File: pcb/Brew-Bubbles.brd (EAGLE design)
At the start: 25.6 x 34.2 mm, 7 parts, among them U1 GP1A57HR

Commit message: JsonConfig working (mostly)
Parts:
- renumbered AMBIENT to ROOM
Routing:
- net 3V3: track 86.2 -> 90.4 mm
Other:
- board size 25.6 x 34.2 mm -> 25.5 x 28.7 mm
- board text added: "Brew Bubbles by @LBussy www.brewbubbles.com"

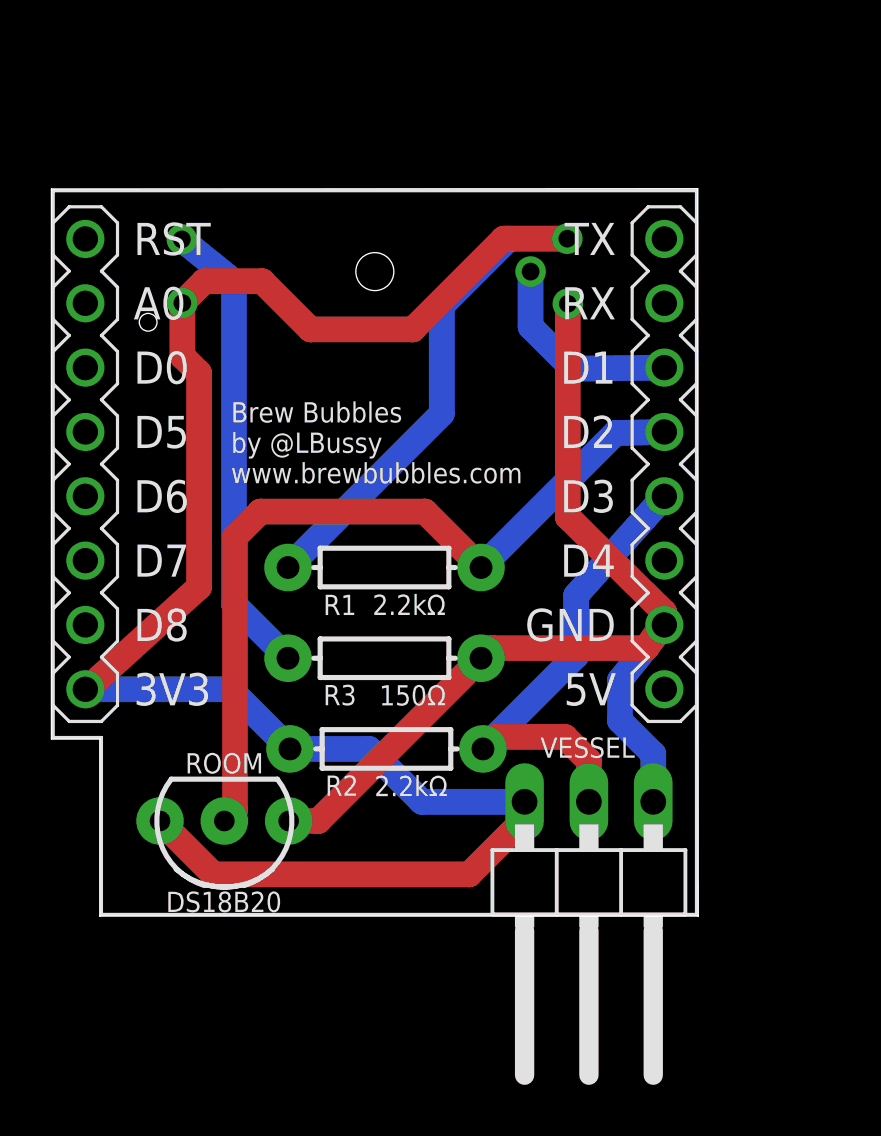
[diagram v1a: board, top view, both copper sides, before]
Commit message: Update PCB, add README
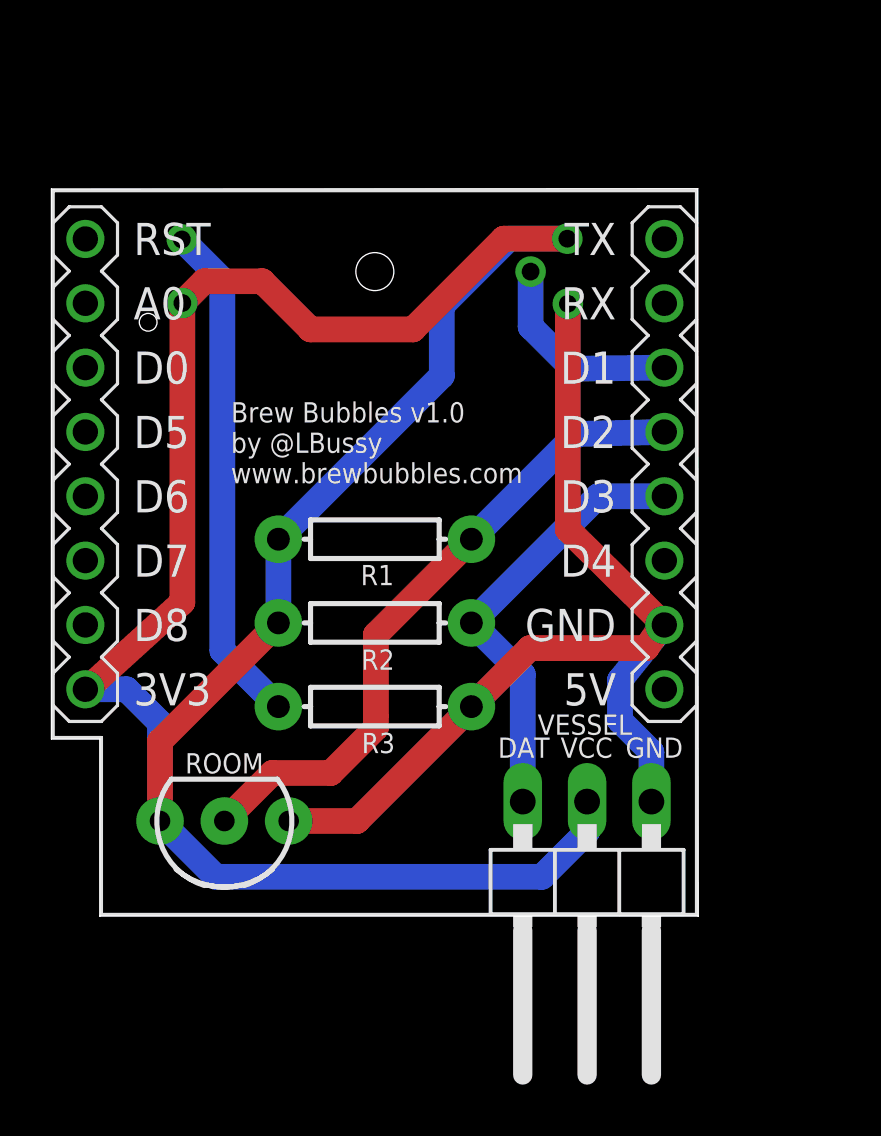
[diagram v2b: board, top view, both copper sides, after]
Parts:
- U2: value WEMOS-D1-MINI-SHIELD -> WEMOS-D1-MINI
- moved R2 5.00 mm to (12.8, 11.6)
- moved R3 1.95 mm to (12.8, 8.30)
- moved R1 1.18 mm to (12.8, 14.9)
- moved VESSEL 0.07 mm to (21.2, 0.74)
- renumbered U$2 to U2
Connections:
- net 3V3: now also VESSEL.2; no longer VESSEL.3
- net D3: now also VESSEL.3; no longer VESSEL.2
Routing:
- net D2: track 31.9 -> 25.9 mm
- net 3V3: track 90.4 -> 92.9 mm
- net D3: track 19.2 -> 17.6 mm
- net PD1: track 18.4 -> 20.0 mm
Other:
- board text added: "Brew Bubbles v1.0 by @LBussy www.brewbubbles.com"
- board text added: "DAT"
- board text added: "GND"
- board text added: "VCC"
- board text removed: "Brew Bubbles by @LBussy www.brewbubbles.com"

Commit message: Update PCD, remove acid traps
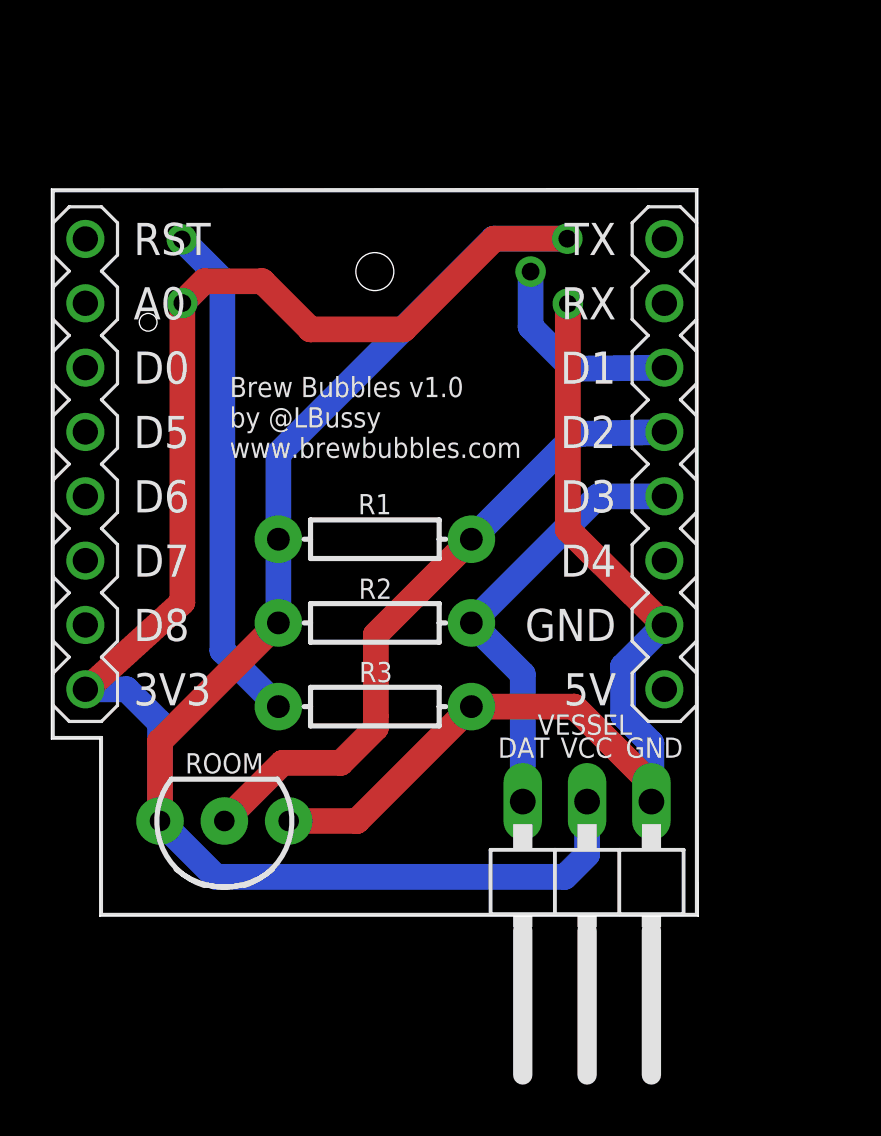
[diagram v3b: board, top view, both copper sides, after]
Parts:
- R1, R2: value 2.2kΩ -> 330
- R3: value 150Ω -> 330
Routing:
- net 3V3: track 92.9 -> 93.8 mm
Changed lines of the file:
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@@
 <drawing>
 <settings>
-<setting alwaysvectorfont="yes"/>
+<setting alwaysvectorfont="no"/>
 <setting verticaltext="up"/>
 </settings>
@@
 </layers>
 <board>
-<fusionsync huburn="a.cGVyc29uYWw6dWUyODZkMjAz" projecturn="a.cGVyc29uYWw6dWUyODZkMjAzI0QyMDE2MTExMzUwODExODUx" f3durn="urn:adsk.wipprod:dm.lineage:MLlsr9vlTViqnB-TMc0w0w" pcbguid="9daba508-4cd0-4a0c-8a93-8bf912c45092" lastpulledtime="" lastsyncedchangeguid="327ecc73-655b-5c8d-87e6-91b64e58cd54"/>
+<fusionsync huburn="a.cGVyc29uYWw6dWUyODZkMjAz" projecturn="a.cGVyc29uYWw6dWUyODZkMjAzI0QyMDE2MTExMzUwODExODUx" f3durn="urn:adsk.wipprod:dm.lineage:MLlsr9vlTViqnB-TMc0w0w" pcbguid="9daba508-4cd0-4a0c-8a93-8bf912c45092" lastpulledtime="" lastsyncedchangeguid="227e19ab-8c40-ec9c-751c-eb66027dfc6e"/>
 <plain>
 <wire x1="1.94" y1="0.03" x2="1.94" y2="7.02" width="0" layer="20"/>
@@
 <wire x1="1.94" y1="0.03" x2="25.57" y2="0.03" width="0" layer="20"/>
 <wire x1="0.03" y1="28.74" x2="25.55" y2="28.75" width="0" layer="20"/>
-<text x="7.12" y="17.12" size="0.8" layer="25" font="vector" ratio="14">Brew Bubbles v1.0
+<text x="7.06840625" y="18.12" size="0.8" layer="25" font="vector" ratio="14">Brew Bubbles v1.0
 by @LBussy
 www.brewbubbles.com</text>
@@
 </element>
 <element name="U2" library="diy-modules" package="WEMOS-D1-MINI-SHIELD" value="WEMOS-D1-MINI" x="12.8" y="14.7" smashed="yes"/>
-<element name="R1" library="SparkFun-Resistors" library_urn="urn:adsk.eagle:library:532" package="AXIAL-0.3" package3d_urn="urn:adsk.eagle:package:39658/1" value="2.2kΩ" x="12.8013" y="14.91" smashed="yes" rot="R180">
-<attribute name="NAME" x="12.2413" y="13.894" size="0.8" layer="25" font="vector" ratio="14" rot="R180" align="bottom-right"/>
+<element name="R1" library="SparkFun-Resistors" package="AXIAL-0.3" value="330" x="12.8013" y="14.91" smashed="yes" rot="R180">
+<attribute name="NAME" x="12.1413" y="16.694" size="0.8" layer="25" font="vector" ratio="14" rot="R180" align="bottom-right"/>
 <attribute name="PROD_ID" value="RES-8371" x="12.8013" y="14.91" size="1.778" layer="27" rot="R180" display="off"/>
 </element>
 <element name="VESSEL" library="pinhead" library_urn="urn:adsk.eagle:library:325" package="1X03/90" package3d_urn="urn:adsk.eagle:package:22459/2" value="3PIN90" x="21.18" y="0.74" smashed="yes" rot="R180">
 <attribute name="NAME" x="19.2274" y="7.1888" size="0.8" layer="25" font="vector" ratio="10"/>
-</element>
-<element name="R2" library="SparkFun-Resistors" library_urn="urn:adsk.eagle:library:532" package="AXIAL-0.3" package3d_urn="urn:adsk.eagle:package:39658/1" value="2.2kΩ" x="12.8013" y="11.6054" smashed="yes" rot="R180">
-<attribute name="NAME" x="12.2625" y="10.556" size="0.8" layer="25" font="vector" ratio="14" rot="R180" align="bottom-right"/>
+<attribute name="POPULARITY" value="17" x="21.18" y="0.74" size="1.778" layer="27" rot="R180" display="off"/>
+</element>
+<element name="R2" library="SparkFun-Resistors" package="AXIAL-0.3" value="330" x="12.8013" y="11.6054" smashed="yes" rot="R180">
+<attribute name="NAME" x="12.1625" y="13.356" size="0.8" layer="25" font="vector" ratio="14" rot="R180" align="bottom-right"/>
 <attribute name="PROD_ID" value="RES-8371" x="12.8013" y="11.6054" size="1.778" layer="27" rot="R180" display="off"/>
 </element>
 <element name="U1" library="SparkFun-Sensors" package="GP1A57HR" value="GP1A57HR" x="12.8" y="25.4762" smashed="yes" rot="MR180">
-<attribute name="NAME" x="12.76" y="24.1142" size="0.8" layer="26" font="vector" ratio="14" rot="MR180" align="bottom-center"/>
+<attribute name="NAME" x="12.81" y="22.1142" size="0.8" layer="26" font="vector" ratio="14" rot="MR180" align="bottom-center"/>
 <attribute name="SF_ID" value="SEN-09299" x="12.8" y="25.4762" size="1.778" layer="28" rot="MR180" display="off"/>
-<attribute name="VALUE" x="12.78" y="26.9182" size="0.8" layer="26" font="vector" ratio="14" rot="MR180" align="top-center"/>
-</element>
-<element name="R3" library="SparkFun-Resistors" library_urn="urn:adsk.eagle:library:532" package="AXIAL-0.3" package3d_urn="urn:adsk.eagle:package:39658/1" value="150Ω" x="12.8013" y="8.3008" smashed="yes" rot="R180">
-<attribute name="NAME" x="12.2813" y="7.2648" size="0.8" layer="25" font="vector" ratio="14" rot="R180" align="bottom-right"/>
+</element>
+<element name="R3" library="SparkFun-Resistors" package="AXIAL-0.3" value="330" x="12.8013" y="8.3008" smashed="yes" rot="R180">
+<attribute name="NAME" x="12.1813" y="10.0648" size="0.8" layer="25" font="vector" ratio="14" rot="R180" align="bottom-right"/>
 <attribute name="PROD_ID" value="RES-8371" x="12.8013" y="8.3008" size="1.778" layer="27" rot="R180" display="off"/>
 </element>
@@
 <wire x1="24.23" y1="11.525696875" x2="20.42" y2="15.291496875" width="1.016" layer="1"/>
 <wire x1="20.42" y1="15.291496875" x2="20.42" y2="24.2062" width="1.016" layer="1"/>
-<wire x1="23.5199" y1="10.6108" x2="18.9213" y2="10.6108" width="1.016" layer="1"/>
-<wire x1="16.6113" y1="8.3008" x2="18.9213" y2="10.6108" width="1.016" layer="1"/>
-<wire x1="24.137203125" y1="11.525" x2="24.23" y2="11.525" width="1.016" layer="1"/>
-<wire x1="24.137203125" y1="11.525" x2="23.5199" y2="10.6108" width="1.016" layer="1"/>
 <wire x1="9.398" y1="3.7846" x2="12.0951" y2="3.7846" width="1.016" layer="1"/>
 <wire x1="12.0951" y1="3.7846" x2="16.6113" y2="8.3008" width="1.016" layer="1"/>
-<wire x1="24.23" y1="11.525" x2="22.479" y2="9.3472" width="1.016" layer="16"/>
-<wire x1="22.479" y1="9.3472" x2="22.479" y2="7.747" width="1.016" layer="16"/>
-<wire x1="22.479" y1="7.747" x2="23.72" y2="6.506" width="1.016" layer="16"/>
-<wire x1="23.72" y1="6.506" x2="23.72" y2="4.55" width="1.016" layer="16"/>
+<wire x1="23.72" y1="4.55" x2="23.72" y2="6.85" width="1.016" layer="16"/>
+<wire x1="23.72" y1="6.85" x2="22.6" y2="7.97" width="1.016" layer="16"/>
+<wire x1="22.6" y1="9.895" x2="24.23" y2="11.525" width="1.016" layer="16"/>
+<wire x1="22.6" y1="7.97" x2="22.6" y2="9.895" width="1.016" layer="16"/>
+<wire x1="16.6113" y1="8.3008" x2="20.6692" y2="8.3008" width="1.016" layer="1"/>
+<wire x1="23.72" y1="5.25" x2="20.6692" y2="8.3008" width="1.016" layer="1"/>
+<wire x1="23.72" y1="5.25" x2="23.72" y2="4.55" width="1.016" layer="1"/>
 </signal>
 <signal name="3V3">
@@
 <contactref element="R1" pad="P$2"/>
 <contactref element="ROOM" pad="3"/>
-<wire x1="8.9913" y1="14.91" x2="15.4432" y2="21.3619" width="1.016" layer="16"/>
-<wire x1="15.4432" y1="21.3619" x2="15.4432" y2="24.13" width="1.016" layer="16"/>
-<wire x1="18.0894" y1="26.7762" x2="20.4" y2="26.7762" width="1.016" layer="16"/>
-<wire x1="15.4432" y1="24.13" x2="18.0894" y2="26.7762" width="1.016" layer="16"/>
+<wire x1="17.4894" y1="26.7762" x2="8.9913" y2="18.2781" width="1.016" layer="16"/>
+<wire x1="8.9913" y1="14.91" x2="8.9913" y2="18.2781" width="1.016" layer="16"/>
+<wire x1="17.4894" y1="26.7762" x2="20.4" y2="26.7762" width="1.016" layer="16"/>
 <wire x1="5.2" y1="24.2362" x2="5.2" y2="12.42035" width="1.016" layer="1"/>
 <wire x1="5.2" y1="12.42035" x2="1.37383125" y2="8.9408" width="1.016" layer="1"/>
@@
 <wire x1="5.2" y1="24.2362" x2="6.06" y2="25.0962" width="1.016" layer="1"/>
 <wire x1="8.3556" y1="25.0962" x2="10.2588" y2="23.193" width="1.016" layer="1"/>
-<wire x1="10.2588" y1="23.193" x2="14.303" y2="23.193" width="1.016" layer="1"/>
-<wire x1="17.8862" y1="26.7762" x2="20.4" y2="26.7762" width="1.016" layer="1"/>
-<wire x1="14.303" y1="23.193" x2="17.8862" y2="26.7762" width="1.016" layer="1"/>
+<wire x1="10.2588" y1="23.193" x2="13.933" y2="23.193" width="1.016" layer="1"/>
+<wire x1="17.5162" y1="26.7762" x2="20.4" y2="26.7762" width="1.016" layer="1"/>
+<wire x1="13.933" y1="23.193" x2="17.5162" y2="26.7762" width="1.016" layer="1"/>
 <contactref element="VESSEL" pad="2"/>
 <wire x1="8.9913" y1="14.91" x2="8.9913" y2="11.6054" width="1.016" layer="16"/>
@@
 <wire x1="2.995" y1="8.985" x2="4.318" y2="7.662" width="1.016" layer="16"/>
 <wire x1="4.318" y1="3.7846" x2="6.5226" y2="1.58" width="1.016" layer="16"/>
-<wire x1="19.4" y1="1.58" x2="21.18" y2="3.36" width="1.016" layer="16"/>
-<wire x1="21.18" y1="3.36" x2="21.18" y2="4.55" width="1.016" layer="16"/>
-<wire x1="6.5226" y1="1.58" x2="19.4" y2="1.58" width="1.016" layer="16"/>
+<wire x1="20.3" y1="1.58" x2="21.18" y2="2.46" width="1.016" layer="16"/>
+<wire x1="21.18" y1="2.46" x2="21.18" y2="4.55" width="1.016" layer="16"/>
+<wire x1="6.5226" y1="1.58" x2="20.3" y2="1.58" width="1.016" layer="16"/>
 </signal>
 <signal name="D2">
@@
 <wire x1="16.6113" y1="14.91" x2="20.76694375" y2="19.06564375" width="1.016" layer="16"/>
 <wire x1="20.76694375" y1="19.06564375" x2="24.23" y2="19.145" width="1.016" layer="16"/>
-<wire x1="6.858" y1="3.7846" x2="8.7534" y2="5.68" width="1.016" layer="1"/>
-<wire x1="8.7534" y1="5.68" x2="11.06" y2="5.68" width="1.016" layer="1"/>
-<wire x1="11.06" y1="5.68" x2="12.84" y2="7.46" width="1.016" layer="1"/>
+<wire x1="6.858" y1="3.7846" x2="9.1534" y2="6.08" width="1.016" layer="1"/>
+<wire x1="9.1534" y1="6.08" x2="11.46" y2="6.08" width="1.016" layer="1"/>
+<wire x1="11.46" y1="6.08" x2="12.84" y2="7.46" width="1.016" layer="1"/>
 <wire x1="12.84" y1="7.46" x2="12.84" y2="7.88" width="1.016" layer="1"/>
 <wire x1="12.84" y1="7.88" x2="12.84" y2="7.98" width="0.1524" layer="1"/>
@@
 <wire x1="21.6109" y1="16.605" x2="16.6113" y2="11.6054" width="1.016" layer="16"/>
 <contactref element="VESSEL" pad="3"/>
-<wire x1="16.6113" y1="11.6054" x2="18.64" y2="9.5767" width="1.016" layer="16"/>
-<wire x1="18.64" y1="9.5767" x2="18.64" y2="4.55" width="1.016" layer="16"/>
+<wire x1="18.64" y1="4.55" x2="18.64" y2="9.5767" width="1.016" layer="16"/>
+<wire x1="18.64" y1="9.5767" x2="16.6113" y2="11.6054" width="1.016" layer="16"/>
 </signal>
 <signal name="D1">
